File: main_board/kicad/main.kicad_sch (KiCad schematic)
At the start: 13 parts, among them J1 Sensorbuchse, J2 Motorbuchse, J3 Motorbuchse, J4 Batteriebuchse, J5 Conn_02x07_Odd_Even, J6 Sensorbuchse

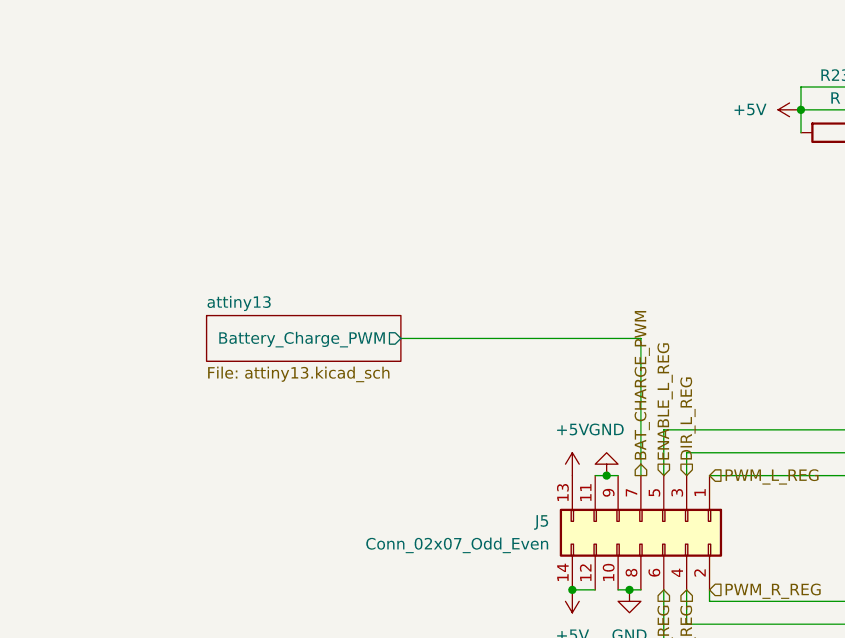
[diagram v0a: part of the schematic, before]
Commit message: added ISP socket for attiny
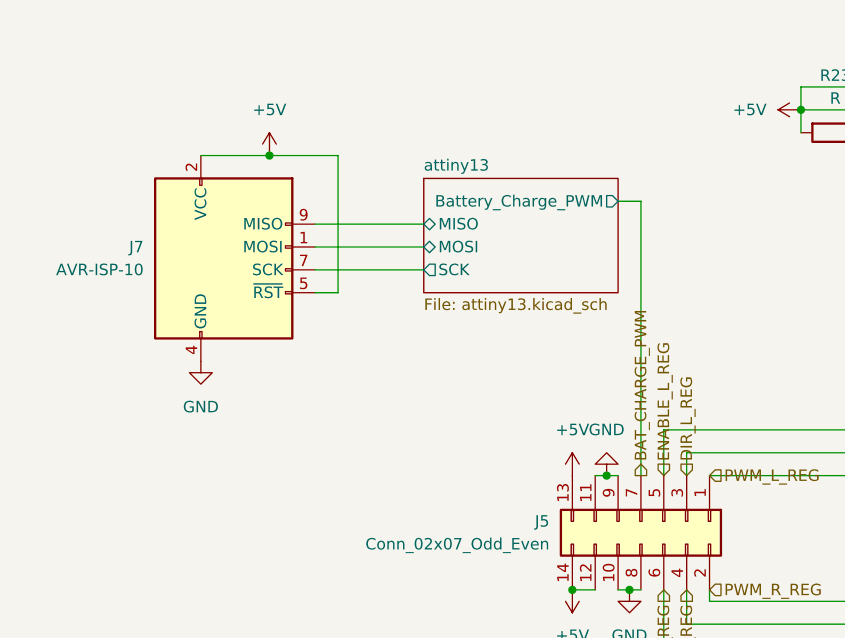
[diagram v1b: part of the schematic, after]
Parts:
- added J7: AVR-ISP-10, Connector_IDC:IDC-Header_2x05_P2.54mm_Vertical, symbol Connector:AVR-ISP-10
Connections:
- net +5V: now also J7.2 (VCC), J7.5 (~{RST})
- net GND: now also J7.10 (GND), J7.4 (GND), J7.6 (GND), J7.8 (GND)
- new net attiny13/MISO: J7.9 (MISO)
- new net attiny13/MOSI: J7.1 (MOSI)
- new net attiny13/SCK: J7.7 (SCK)
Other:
- sheet attiny13 ports: added MISO, MOSI, SCK; removed none
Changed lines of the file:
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@@
   (junction (at 137.16 143.51) (diameter 0) (color 0 0 0 0)
   )
+  (junction (at 45.085 60.96) (diameter 0) (color 0 0 0 0)
+  )
   (junction (at 78.74 109.22) (diameter 0) (color 0 0 0 0)
   )
@@
     (stroke (width 0) (type default))
   )
-  (wire (pts (xy 86.36 96.52) (xy 86.36 81.28))
+  (wire (pts (xy 86.36 96.52) (xy 86.36 66.04))
     (stroke (width 0) (type default))
   )
@@
     (stroke (width 0) (type default))
   )
+  (wire (pts (xy 50.165 68.58) (xy 62.23 68.58))
+    (stroke (width 0) (type default))
+  )
   (wire (pts (xy 104.14 53.34) (xy 104.14 55.88))
     (stroke (width 0) (type default))
@@
     (stroke (width 0) (type default))
   )
+  (wire (pts (xy 52.705 76.2) (xy 52.705 60.96))
+    (stroke (width 0) (type default))
+  )
   (wire (pts (xy 129.54 140.97) (xy 139.7 140.97))
     (stroke (width 0) (type default))
@@
     (stroke (width 0) (type default))
   )
+  (wire (pts (xy 50.165 71.12) (xy 62.23 71.12))
+    (stroke (width 0) (type default))
+  )
   (wire (pts (xy 186.69 85.09) (xy 204.47 85.09))
     (stroke (width 0) (type default))
@@
     (stroke (width 0) (type default))
   )
-  (wire (pts (xy 86.36 81.28) (xy 59.69 81.28))
+  (wire (pts (xy 86.36 66.04) (xy 83.82 66.04))
     (stroke (width 0) (type default))
   )
@@
     (stroke (width 0) (type default))
   )
+  (wire (pts (xy 52.705 60.96) (xy 45.085 60.96))
+    (stroke (width 0) (type default))
+  )
   (wire (pts (xy 143.51 146.05) (xy 134.62 146.05))
     (stroke (width 0) (type default))
@@
     (stroke (width 0) (type default))
   )
+  (wire (pts (xy 45.085 60.96) (xy 37.465 60.96))
+    (stroke (width 0) (type default))
+  )
   (wire (pts (xy 143.51 60.96) (xy 142.24 60.96))
     (stroke (width 0) (type default))
@@
     (stroke (width 0) (type default))
   )
+  (wire (pts (xy 50.165 76.2) (xy 52.705 76.2))
+    (stroke (width 0) (type default))
+  )
   (wire (pts (xy 91.44 93.98) (xy 143.51 93.98))
     (stroke (width 0) (type default))
@@
   )
   (wire (pts (xy 139.7 123.19) (xy 143.51 123.19))
+    (stroke (width 0) (type default))
+  )
+  (wire (pts (xy 50.165 73.66) (xy 62.23 73.66))
     (stroke (width 0) (type default))
   )
@@
         (path "/9139d8e7-a5dc-421f-9a12-f77d83384a16"
           (reference "R21") (unit 1)
+        )
+      )
+    )
+  )
+  (symbol (lib_id "power:GND") (at 37.465 83.82 0) (unit 1)
+    (in_bom yes) (on_board yes) (dnp no) (fields_autoplaced)
+    (property "Reference" "#PWR044" (at 37.465 90.17 0)
+      (effects (font (size 1.27 1.27)) hide)
+    )
+    (property "Value" "GND" (at 37.465 88.9 0)
+      (effects (font (size 1.27 1.27)))
+    )
+    (property "Footprint" "" (at 37.465 83.82 0)
+      (effects (font (size 1.27 1.27)) hide)
+    )
+    (property "Datasheet" "" (at 37.465 83.82 0)
+      (effects (font (size 1.27 1.27)) hide)
+    )
+    (pin "1")
+    (instances
+      (project "main"
+        (path "/9139d8e7-a5dc-421f-9a12-f77d83384a16"
+          (reference "#PWR044") (unit 1)
         )
       )
@@
     )
   )
+  (symbol (lib_id "Connector:AVR-ISP-10") (at 40.005 73.66 0) (unit 1)
+    (in_bom yes) (on_board yes) (dnp no) (fields_autoplaced)
+    (property "Reference" "J7" (at 31.115 71.12 0)
+      (effects (font (size 1.27 1.27)) (justify right))
+    )
+    (property "Value" "AVR-ISP-10" (at 31.115 73.66 0)
+      (effects (font (size 1.27 1.27)) (justify right))
+    )
+    (property "Footprint" "Connector_IDC:IDC-Header_2x05_P2.54mm_Vertical" (at 33.655 72.39 90)
+      (effects (font (size 1.27 1.27)) hide)
+    )
+    (property "Datasheet" " ~" (at 7.62 87.63 0)
+      (effects (font (size 1.27 1.27)) hide)
+    )
+    (pin "1")
+    (pin "10")
+    (pin "2")
+    (pin "3")
+    (pin "4")
+    (pin "5")
+    (pin "6")
+    (pin "7")
+    (pin "8")
+    (pin "9")
+    (instances
+      (project "main"
+        (path "/9139d8e7-a5dc-421f-9a12-f77d83384a16"
+          (reference "J7") (unit 1)
+        )
+      )
+    )
+  )
   (symbol (lib_id "Device:R") (at 116.84 55.88 270) (unit 1)
     (in_bom yes) (on_board yes) (dnp no) (fields_autoplaced)
@@
         (path "/9139d8e7-a5dc-421f-9a12-f77d83384a16"
           (reference "R23") (unit 1)
+        )
+      )
+    )
+  )
+  (symbol (lib_id "power:+5V") (at 45.085 60.96 0) (unit 1)
+    (in_bom yes) (on_board yes) (dnp no) (fields_autoplaced)
+    (property "Reference" "#PWR043" (at 45.085 64.77 0)
+      (effects (font (size 1.27 1.27)) hide)
+    )
+    (property "Value" "+5V" (at 45.085 55.88 0)
+      (effects (font (size 1.27 1.27)))
+    )
+    (property "Footprint" "" (at 45.085 60.96 0)
+      (effects (font (size 1.27 1.27)) hide)
+    )
+    (property "Datasheet" "" (at 45.085 60.96 0)
+      (effects (font (size 1.27 1.27)) hide)
+    )
+    (pin "1")
+    (instances
+      (project "main"
+        (path "/9139d8e7-a5dc-421f-9a12-f77d83384a16"
+          (reference "#PWR043") (unit 1)
         )
       )
@@
     )
   )
-  (sheet (at 38.1 78.74) (size 21.59 5.08) (fields_autoplaced)
+  (sheet (at 62.23 63.5) (size 21.59 12.7) (fields_autoplaced)
     (stroke (width 0.1524) (type solid))
     (fill (color 0 0 0 0.0000))
-    (property "Sheetname" "attiny13" (at 38.1 78.0284 0)
+    (property "Sheetname" "attiny13" (at 62.23 62.7884 0)
       (effects (font (size 1.27 1.27)) (justify left bottom))
     )
-    (property "Sheetfile" "attiny13.kicad_sch" (at 38.1 84.4046 0)
+    (property "Sheetfile" "attiny13.kicad_sch" (at 62.23 76.7846 0)
       (effects (font (size 1.27 1.27)) (justify left top))
     )
-    (pin "Battery_Charge_PWM" output (at 59.69 81.28 0)
+    (pin "Battery_Charge_PWM" output (at 83.82 66.04 0)
       (effects (font (size 1.27 1.27)) (justify right))
     )
-    (instances
+    (pin "SCK" output (at 62.23 73.66 180)
+      (effects (font (size 1.27 1.27)) (justify left))
+    )
+    (pin "MOSI" bidirectional (at 62.23 71.12 180)
+      (effects (font (size 1.27 1.27)) (justify left))
+    )
+    (pin "MISO" bidirectional (at 62.23 68.58 180)
+      (effects (font (size 1.27 1.27)) (justify left))
+    )
+    (instances

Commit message: added pull up resistor values
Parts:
- R21, R22, R23, R24, R25, R43: value R -> 50k
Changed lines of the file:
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@@
       (effects (font (size 1.27 1.27)))
     )
-    (property "Value" "R" (at 125.73 137.16 90)
+    (property "Value" "50k" (at 125.73 137.16 90)
       (effects (font (size 1.27 1.27)))
     )
@@
       (effects (font (size 1.27 1.27)))
     )
-    (property "Value" "R" (at 125.73 49.53 90)
+    (property "Value" "50k" (at 125.73 49.53 90)
       (effects (font (size 1.27 1.27)))
     )
@@
       (effects (font (size 1.27 1.27)))
     )
-    (property "Value" "R" (at 116.84 139.7 90)
+    (property "Value" "50k" (at 116.84 139.7 90)
       (effects (font (size 1.27 1.27)))
     )
@@
       (effects (font (size 1.27 1.27)))
     )
-    (property "Value" "R" (at 116.84 52.07 90)
+    (property "Value" "50k" (at 116.84 52.07 90)
       (effects (font (size 1.27 1.27)))
     )
@@
       (effects (font (size 1.27 1.27)))
     )
-    (property "Value" "R" (at 106.68 142.24 90)
+    (property "Value" "50k" (at 106.68 142.24 90)
       (effects (font (size 1.27 1.27)))
     )
@@
       (effects (font (size 1.27 1.27)))
     )
-    (property "Value" "R" (at 107.95 54.61 90)
-      (effects (font (size 1.27 1.27)))
-    )
+    (property "Value" "50k" (at 107.95 54.61 90)
+      (effects (font (size 1.27 1.27)))
+    )

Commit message: fixed pull up resistor values
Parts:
- R21, R22, R23, R24, R25, R43: value 50k -> 30k
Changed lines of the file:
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@@
       (effects (font (size 1.27 1.27)))
     )
-    (property "Value" "50k" (at 125.73 137.16 90)
+    (property "Value" "30k" (at 125.73 137.16 90)
       (effects (font (size 1.27 1.27)))
     )
@@
       (effects (font (size 1.27 1.27)))
     )
-    (property "Value" "50k" (at 125.73 49.53 90)
+    (property "Value" "30k" (at 125.73 49.53 90)
       (effects (font (size 1.27 1.27)))
     )
@@
       (effects (font (size 1.27 1.27)))
     )
-    (property "Value" "50k" (at 116.84 139.7 90)
+    (property "Value" "30k" (at 116.84 139.7 90)
       (effects (font (size 1.27 1.27)))
     )
@@
       (effects (font (size 1.27 1.27)))
     )
-    (property "Value" "50k" (at 116.84 52.07 90)
+    (property "Value" "30k" (at 116.84 52.07 90)
       (effects (font (size 1.27 1.27)))
     )
@@
       (effects (font (size 1.27 1.27)))
     )
-    (property "Value" "50k" (at 106.68 142.24 90)
+    (property "Value" "30k" (at 106.68 142.24 90)
       (effects (font (size 1.27 1.27)))
     )
@@
       (effects (font (size 1.27 1.27)))
     )
-    (property "Value" "50k" (at 107.95 54.61 90)
-      (effects (font (size 1.27 1.27)))
-    )
+    (property "Value" "30k" (at 107.95 54.61 90)
+      (effects (font (size 1.27 1.27)))
+    )

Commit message: renamed motor magic file
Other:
- sheet MotorMagic: file untitled.kicad_sch -> MotorMagic.kicad_sch
- sheet MotorMagic1: file untitled.kicad_sch -> MotorMagic.kicad_sch
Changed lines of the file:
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@@
+    )
+  )
+  (sheet (at 143.51 107.95) (size 43.18 22.86) (fields_autoplaced)
+    (stroke (width 0.1524) (type solid))
+    (fill (color 0 0 0 0.0000))
+    (property "Sheetname" "MotorMagic1" (at 143.51 107.2384 0)
+      (effects (font (size 1.27 1.27)) (justify left bottom))
+    )
+    (property "Sheetfile" "MotorMagic.kicad_sch" (at 143.51 131.3946 0)
+      (effects (font (size 1.27 1.27)) (justify left top))
+    )
+    (pin "PWM" input (at 143.51 110.49 180)
+      (effects (font (size 1.27 1.27)) (justify left))
+    )
+    (pin "{slash}ENABLE" input (at 143.51 115.57 180)
+      (effects (font (size 1.27 1.27)) (justify left))
+    )
+    (pin "HAL3" input (at 143.51 128.27 180)
+      (effects (font (size 1.27 1.27)) (justify left))
+    )
+    (pin "HAL1" input (at 143.51 123.19 180)
+      (effects (font (size 1.27 1.27)) (justify left))
+    )
+    (pin "HAL2" input (at 143.51 125.73 180)
+      (effects (font (size 1.27 1.27)) (justify left))
+    )
+    (pin "DIR" input (at 143.51 113.03 180)
+      (effects (font (size 1.27 1.27)) (justify left))
+    )
+    (pin "B_OUT" output (at 186.69 113.03 0)
+      (effects (font (size 1.27 1.27)) (justify right))
+    )
+    (pin "G_OUT" output (at 186.69 115.57 0)
+      (effects (font (size 1.27 1.27)) (justify right))
+    )
+    (pin "Y_OUT" output (at 186.69 118.11 0)
+      (effects (font (size 1.27 1.27)) (justify right))
+    )
+    (instances
+      (project "main"
+        (path "/9139d8e7-a5dc-421f-9a12-f77d83384a16" (page "4"))
+      )
     )
   )
@@
     )
   )
-  (sheet (at 143.51 107.95) (size 43.18 22.86) (fields_autoplaced)
-    (stroke (width 0.1524) (type solid))
-    (fill (color 0 0 0 0.0000))
-    (property "Sheetname" "MotorMagic1" (at 143.51 107.2384 0)
-      (effects (font (size 1.27 1.27)) (justify left bottom))
-    )
-    (property "Sheetfile" "untitled.kicad_sch" (at 143.51 131.3946 0)
-      (effects (font (size 1.27 1.27)) (justify left top))
-    )
-    (pin "PWM" input (at 143.51 110.49 180)
-      (effects (font (size 1.27 1.27)) (justify left))
-    )
-    (pin "{slash}ENABLE" input (at 143.51 115.57 180)
-      (effects (font (size 1.27 1.27)) (justify left))
-    )
-    (pin "HAL3" input (at 143.51 128.27 180)
-      (effects (font (size 1.27 1.27)) (justify left))
-    )
-    (pin "HAL1" input (at 143.51 123.19 180)
-      (effects (font (size 1.27 1.27)) (justify left))
-    )
-    (pin "HAL2" input (at 143.51 125.73 180)
-      (effects (font (size 1.27 1.27)) (justify left))
-    )
-    (pin "DIR" input (at 143.51 113.03 180)
-      (effects (font (size 1.27 1.27)) (justify left))
-    )
-    (pin "B_OUT" output (at 186.69 113.03 0)
-      (effects (font (size 1.27 1.27)) (justify right))
-    )
-    (pin "G_OUT" output (at 186.69 115.57 0)
-      (effects (font (size 1.27 1.27)) (justify right))
-    )
-    (pin "Y_OUT" output (at 186.69 118.11 0)
-      (effects (font (size 1.27 1.27)) (justify right))
-    )
-    (instances
-      (project "main"
-        (path "/9139d8e7-a5dc-421f-9a12-f77d83384a16" (page "4"))
-      )
-    )
-  )
   (sheet (at 143.51 74.93) (size 43.18 22.86) (fields_autoplaced)
     (stroke (width 0.1524) (type solid))
@@
       (effects (font (size 1.27 1.27)) (justify left bottom))
     )
-    (property "Sheetfile" "untitled.kicad_sch" (at 143.51 98.3746 0)
+    (property "Sheetfile" "MotorMagic.kicad_sch" (at 143.51 98.3746 0)
       (effects (font (size 1.27 1.27)) (justify left top))
     )
